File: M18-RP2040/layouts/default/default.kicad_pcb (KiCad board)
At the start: 2 copper layers, 32 x 37 mm, 39 parts

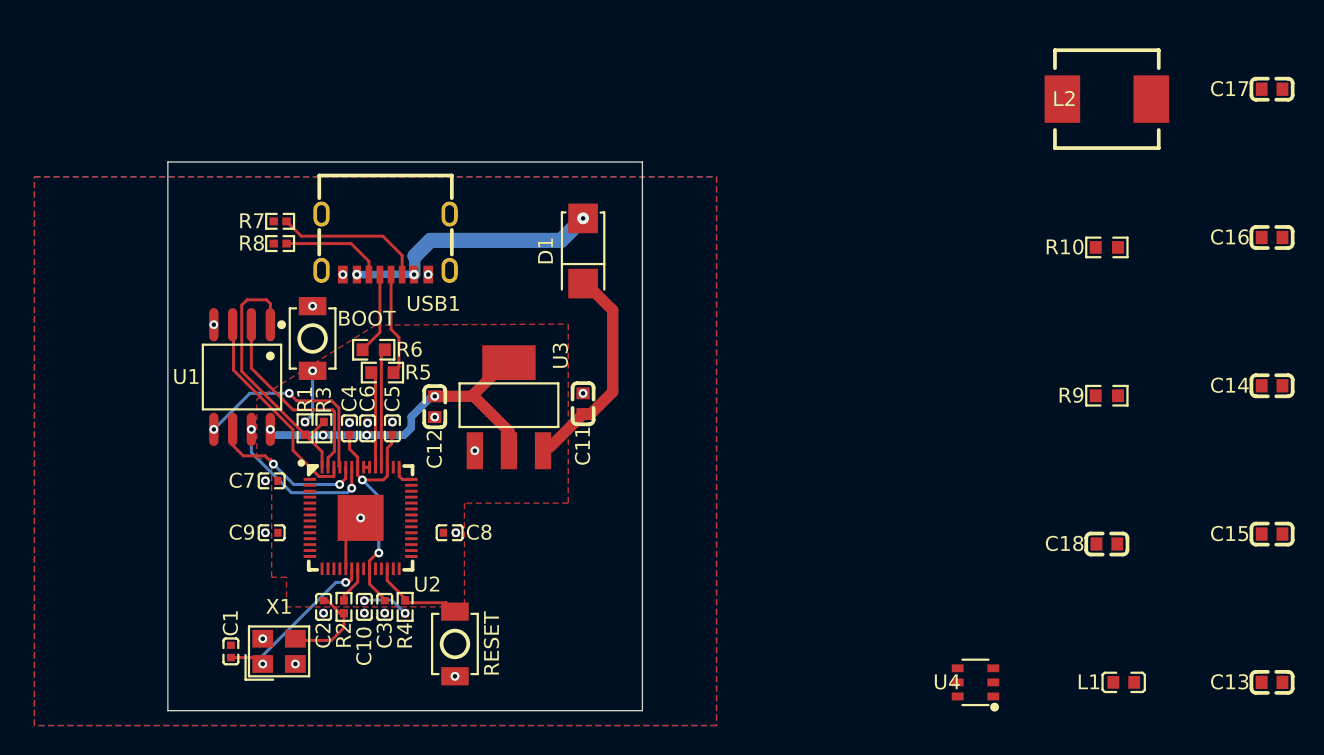
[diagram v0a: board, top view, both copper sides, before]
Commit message: M18 Buck Placement
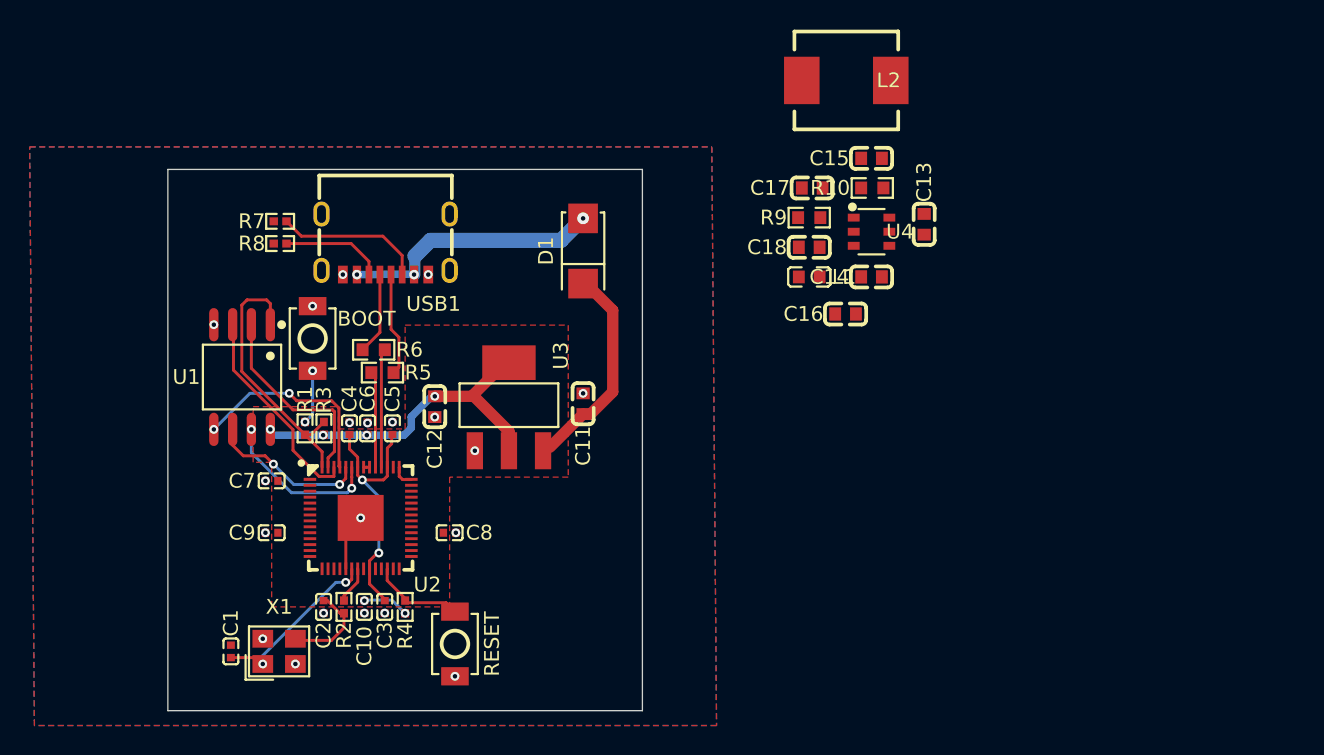
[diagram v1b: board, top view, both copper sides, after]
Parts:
- moved C13 38.8 mm to (118.0, 112.2), turned to -90 degrees
- moved C15 37.0 mm to (114.5, 107.8)
- moved L1 34.6 mm to (110.2, 115.8), turned to 180 degrees
- moved C17 31.7 mm to (110.5, 109.8)
- moved U4 31.2 mm to (114.5, 112.7), turned to 180 degrees
- moved C16 29.2 mm to (112.7, 118.2)
- moved C18 28.3 mm to (110.2, 113.8)
- moved C14 28.0 mm to (114.5, 115.8)
- moved R9 23.4 mm to (110.2, 111.8)
- moved L2 17.6 mm to (112.8, 102.5), turned to 180 degrees
- moved R10 16.3 mm to (114.5, 109.8)
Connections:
- L2 pad 1: (no net) -> lv
- L2 pad 2: (no net) -> fb_cap-power-hv
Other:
- board size 32 x 37 mm -> 32 x 36.5 mm

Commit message: Updated Buck to TI for cost savings
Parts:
- removed L1: , Murata_Electronics_BLM18PG121SN1D:L0603
- added C19: 47µF ±20%, Samsung_Electro_Mechanics_CL31A476MPHNNNE:C1206, F.Cu at (0.00, -70.0)
- added C20: 47µF ±20%, Samsung_Electro_Mechanics_CL31A476MPHNNNE:C1206, F.Cu at (0.00, -80.0)
- added C21: 10nF ±10%, Samsung_Electro_Mechanics_CL05B103KB5NNNC:C0402, F.Cu at (0.00, -110.0)
- added D2: Vf {ℝ+}V, MDD_Microdiode_Electronics_SS34:SMA_L4.3-W2.6-LS5.2-RD, F.Cu at (0.00, 0.00)
- added R11: 30kΩ ±1%, UNI_ROYAL_0603WAF3002T5E:R0603, F.Cu at (0.00, -60.0)
- added R12: 330kΩ ±1%, UNI_ROYAL_0402WGF3303TCE:R0402, F.Cu at (0.00, -90.0)
- added R13: 68kΩ ±1%, UNI_ROYAL_0402WGF6802TCE:R0402, F.Cu at (0.00, -100.0)
- C13: footprint YAGEO_CC0603KRX7R9BB104:C0603 -> Samsung_Electro_Mechanics_CL05B104KO5NNNC:C0402
- C14: value 100nF ±10% -> 10nF ±10%; footprint YAGEO_CC0603KRX7R9BB104:C0603 -> Samsung_Electro_Mechanics_CL05B103KB5NNNC:C0402
- C15: value 10µF ±10% -> 4.7µF ±10%; footprint Samsung_Electro_Mechanics_CL10A106KP8NNNC:C0603 -> FH_1206B475K500NT:C1206
- C16: value 22µF ±20% -> 4.7µF ±10%; footprint Samsung_Electro_Mechanics_CL10A226MQ8NRNC:C0603 -> FH_1206B475K500NT:C1206
- C17: value 22µF ±20% -> 47pF ±5%; footprint Samsung_Electro_Mechanics_CL10A226MQ8NRNC:C0603 -> FH_0402CG470J500NT:C0402
- C18: value 47pF ±5% -> 1nF ±10%; footprint Samsung_Electro_Mechanics_CL10C470JB8NNNC:C0603 -> FH_0402B102K500NT:C0402
- R10: value 22kΩ ±1% -> 1.8kΩ ±1%; footprint UNI_ROYAL_0603WAF2202T5E:R0603 -> UNI_ROYAL_0603WAF1801T5E:R0603
- R9: value 120kΩ ±1% -> 10kΩ ±1%; footprint UNI_ROYAL_0603WAF1203T5E:R0603 -> UNI_ROYAL_0402WGF1002TCE:R0402
- U4: footprint Diodes_Incorporated_AP63301WU_7:TSOT-23-6_L2.9-W1.6-P0.95-LS2.8-BR -> Texas_Instruments_TPS54331DR:SOIC-8_L5.0-W4.0-P1.27-LS6.0-BL
- moved C18 197.4 mm to (0.00, -50.0)
- moved C16 186.2 mm to (0.00, -30.0)
- moved C17 186.1 mm to (0.00, -40.0)
- moved C15 171.5 mm to (0.00, -20.0)
- moved C13 169.9 mm to (0.00, -10.0), turned to 0 degrees
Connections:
- C13 pad 1: bst_cap-power-hv -> boot_cap-power-hv
- C13 pad 2: lv -> cathode
- C16 pad 1: fb_cap-power-hv -> V+
- C17 pad 1: fb_cap-power-hv -> comp_c2-power-hv
- C18 pad 1: fb_cap-power-hv -> comp_c2-power-hv
- C18 pad 2: fb_cap-power-lv -> lv
- L2 pad 1: lv -> cathode
- L2 pad 2: fb_cap-power-hv -> 5V
- R10 pad 1: fb_cap-power-lv -> (no net)
- R10 pad 2: GND -> (no net)
- R9 pad 1: fb_cap-power-hv -> 5V
- R9 pad 2: fb_cap-power-lv -> VSENSE
- U4 pad 1: fb_cap-power-lv -> boot_cap-power-hv
- U4 pad 3: V+ -> EN
- U4 pad 4: GND -> ss_cap-power-hv
- U4 pad 5: lv -> VSENSE
- U4 pad 6: bst_cap-power-hv -> comp_c2-power-hv
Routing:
- net vUSB: track 17.5 -> 0.00 mm, vias 3 -> 0
- net (no net): track 0.00 -> 17.5 mm, vias 0 -> 3
- net ss_cap-power-hv: track 0.00 -> 14.5 mm
- net 5V: track 14.5 -> 0.00 mm
- net boot_cap-power-hv: track 0.00 -> 3.84 mm, vias 0 -> 20
- net GND: track 3.84 -> 0.00 mm, vias 20 -> 0
- added copper zone on B.Cu, net (none)
- added copper zone on F.Cu, net (none)
- removed copper zone on B.Cu, net GND
- removed copper zone on F.Cu, net GND

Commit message: Basic Buck layout
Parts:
- moved C21 279.0 mm to (116.0, 143.8), turned to -90 degrees
- moved R13 267.6 mm to (113.7, 142.3), turned to -90 degrees
- moved R12 256.1 mm to (113.7, 139.5), turned to -90 degrees
- moved R11 240.5 mm to (129.5, 142.6)
- moved C20 240.3 mm to (111.4, 133.0), turned to 180 degrees
- moved C18 230.2 mm to (128.8, 140.8), turned to -90 degrees
- moved C19 229.3 mm to (111.4, 130.4), turned to 180 degrees
- moved C17 222.9 mm to (130.3, 140.8), turned to -90 degrees
- moved C16 198.8 mm to (107.2, 137.4), turned to 90 degrees
- moved C15 192.8 mm to (111.3, 137.4), turned to 90 degrees
- moved D2 187.8 mm to (127.6, 137.9)
- moved C13 186.7 mm to (115.9, 136.3)
- moved R10 34.0 mm to (123.5, 142.5), turned to -90 degrees
- moved R9 33.6 mm to (125.6, 141.7), turned to 180 degrees
- moved L2 31.4 mm to (121.7, 132.6)
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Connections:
- R10 pad 1: (no net) -> VSENSE
- R10 pad 2: (no net) -> GND
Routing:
- net vUSB: track 0.00 -> 17.5 mm, vias 0 -> 3
- net (no net): track 17.5 -> 0.00 mm, vias 3 -> 0
- net ss_cap-power-hv: track 14.5 -> 0.00 mm
- net 5V: track 0.00 -> 14.5 mm
- net boot_cap-power-hv: track 3.84 -> 0.00 mm, vias 20 -> 0
- net GND: track 0.00 -> 3.84 mm, vias 0 -> 20

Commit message: Build clean up and buck routing
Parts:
- moved C13 12.7 mm to (103.2, 135.5)
- moved C21 12.7 mm to (103.3, 142.9)
- moved D2 12.7 mm to (114.8, 137.0)
- moved L2 12.7 mm to (109.0, 131.8)
- moved R10 12.7 mm to (110.8, 141.7)
- moved R12 12.7 mm to (101.0, 138.7)
- moved R13 12.7 mm to (101.0, 141.4)
- moved R9 12.7 mm to (112.9, 140.8)
- moved U4 12.7 mm to (106.0, 138.8)
- moved C17 12.7 mm to (117.6, 140.0)
- moved C18 12.7 mm to (116.1, 140.0)
- moved R11 12.7 mm to (116.8, 141.8)
- moved C14 12.7 mm to (96.6, 137.0)
- moved C15 12.7 mm to (98.6, 137.0)
- moved C16 12.7 mm to (94.5, 137.0)
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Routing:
- net V+: track 0.00 -> 50.5 mm
- net 5V: track 14.5 -> 49.6 mm
- net cathode: track 0.00 -> 17.9 mm
- net comp_c2-power-hv: track 0.00 -> 8.91 mm
- net GND: track 3.84 -> 10.3 mm, vias 20 -> 28
- net EN: track 0.00 -> 4.39 mm
- net vUSB: track 17.5 -> 13.2 mm
- net VSENSE: track 0.00 -> 3.85 mm
- net c_osc_2-power-hv: track 6.38 -> 4.06 mm
- net hv: track 11.7 -> 9.80 mm
- net ss_cap-power-hv: track 0.00 -> 1.77 mm
- net boot_cap-power-hv: track 0.00 -> 1.69 mm
- net lv: track 0.00 -> 1.41 mm
- added copper zone on B.Cu, net GND
- added copper zone on F.Cu, net GND
- removed copper zone on B.Cu, net (none)
- removed copper zone on F.Cu, net (none)
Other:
- board size 32 x 36.5 mm -> 70 x 36 mm

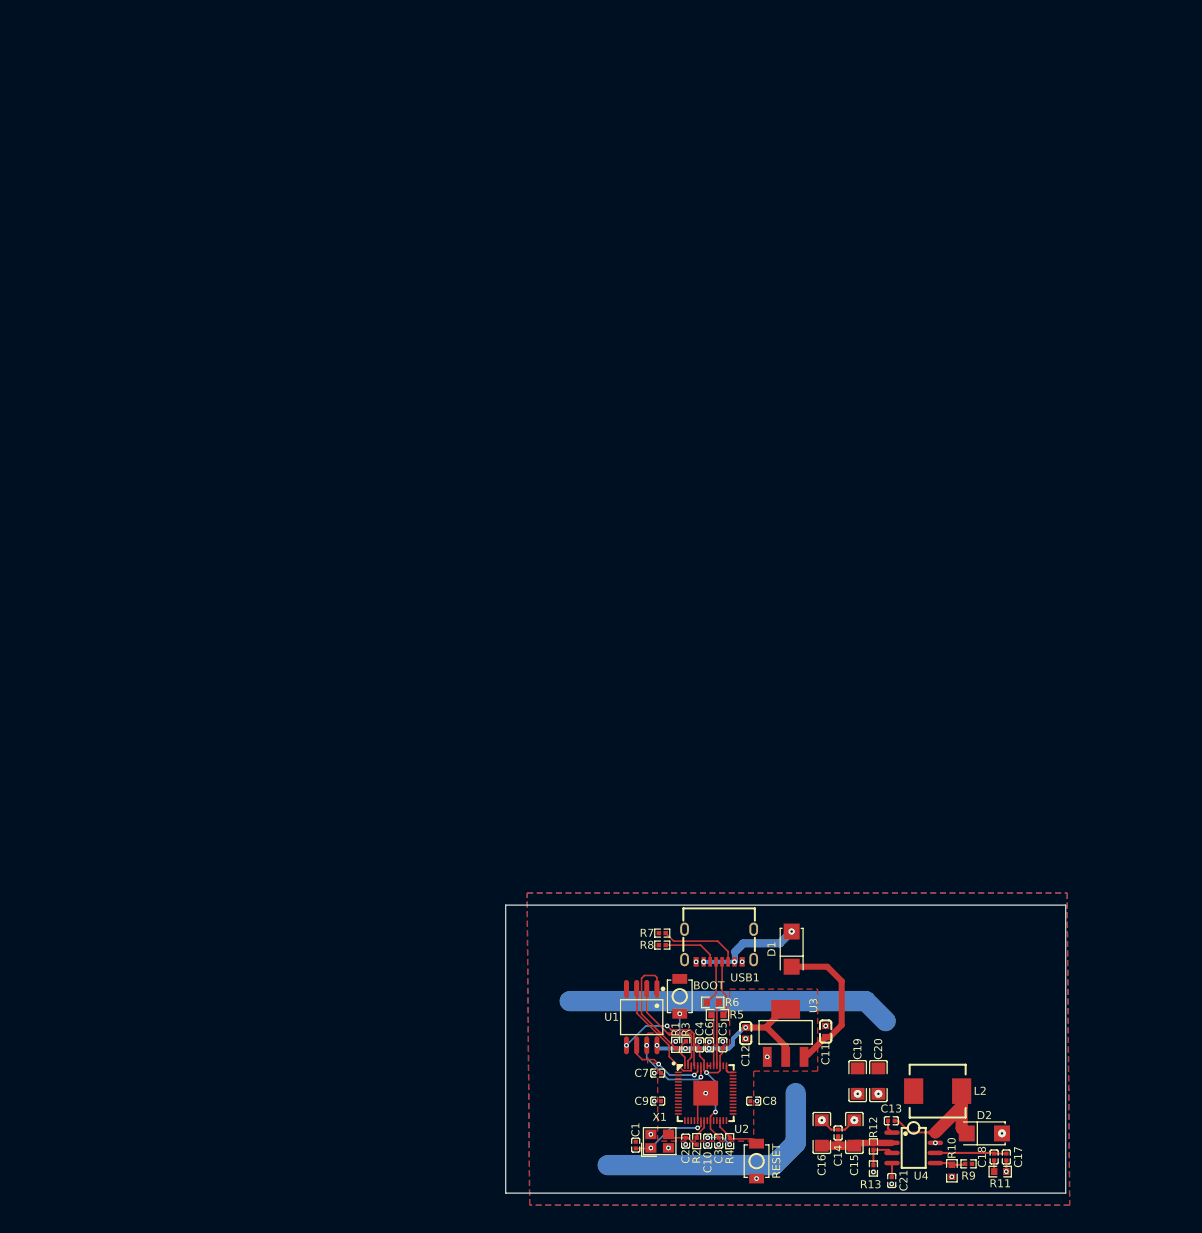
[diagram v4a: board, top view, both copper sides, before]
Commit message: ESP32 New Buck & Header Updates
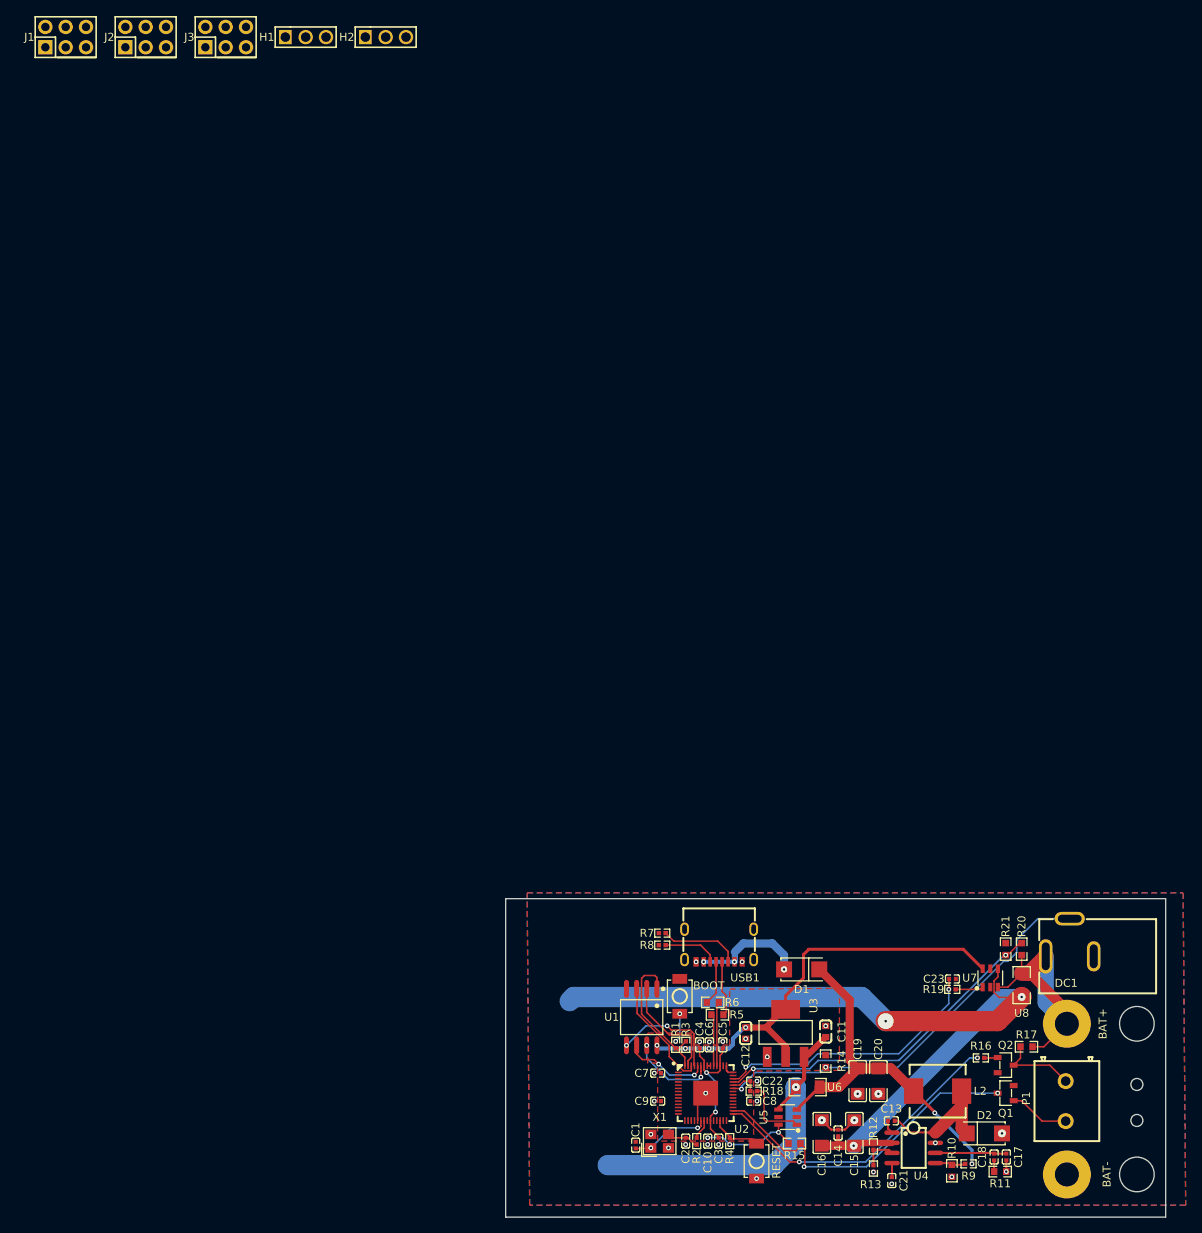
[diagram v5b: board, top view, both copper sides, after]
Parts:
- added BAT+: , m18_10awg_pad:M18_10AWG_PAD, F.Cu at (125.2, 123.3)
- added BAT-: , m18_10awg_pad:M18_10AWG_PAD, F.Cu at (125.2, 142.2)
- added C22: 10nF ±10%, Samsung_Electro_Mechanics_CL05B103KB5NNNC:C0402, F.Cu at (86.0, 130.5)
- added C23: 10nF ±10%, Samsung_Electro_Mechanics_CL05B103KB5NNNC:C0402, F.Cu at (110.8, 117.7)
- added DC1: , CUI_PJ_002BH:DC-IN-TH_PJ-002BH, F.Cu at (125.5, 112.5)
- added H1: , BOOMELE_2_54_1_3P:HDR-TH_3P-P2.54-V-M-1, F.Cu at (30.0, 0.00)
- added H2: , BOOMELE_2_54_1_3P:HDR-TH_3P-P2.54-V-M-1, F.Cu at (40.0, 0.00)
- added J1: , BOOMELE_2_54_2_3P:HDR-TH_6P-P2.54-V-M-R2-C3-S2.54-1, F.Cu at (0.00, 0.00)
- added J2: , BOOMELE_2_54_2_3P:HDR-TH_6P-P2.54-V-M-R2-C3-S2.54-1, F.Cu at (10.0, 0.00)
- added J3: , BOOMELE_2_54_2_3P:HDR-TH_6P-P2.54-V-M-R2-C3-S2.54-1, F.Cu at (20.0, 0.00)
- added P1: , Ningbo_Kangnex_Elec_WJ127_5_0_02P_14_00A:CONN-TH_2P-P5.00_CPC3703CTR, F.Cu at (125.0, 133.0)
- added Q1: , Changjiang_Electronics_Tech_2N7002:SOT-23-3_L2.9-W1.3-P1.90-LS2.4-BR, F.Cu at (117.5, 132.0)
- added Q2: , Changjiang_Electronics_Tech_2N7002:SOT-23-3_L2.9-W1.3-P1.90-LS2.4-BR, F.Cu at (117.5, 128.5)
- added R14: 10kΩ ±1%, UNI_ROYAL_0603WAF1002T5E:R0603, F.Cu at (95.0, 128.0)
- added R15: 10kΩ ±1%, UNI_ROYAL_0603WAF1002T5E:R0603, F.Cu at (91.1, 138.3)
- added R16: 330Ω ±1%, UNI_ROYAL_0402WGF3300TCE:R0402, F.Cu at (114.4, 127.6)
- added R17: 10kΩ ±1%, UNI_ROYAL_0603WAF1002T5E:R0603, F.Cu at (120.1, 126.2)
- added R18: 220Ω ±1%, UNI_ROYAL_0402WGF2200TCE:R0402, F.Cu at (86.0, 131.8)
- added R19: 220Ω ±1%, UNI_ROYAL_0402WGF2200TCE:R0402, F.Cu at (110.8, 119.0)
- added R20: 150kΩ ±1%, UNI_ROYAL_0603WAF1503T5E:R0603, F.Cu at (119.5, 114.0)
- added R21: 22kΩ ±1%, UNI_ROYAL_0603WAF2202T5E:R0603, F.Cu at (117.5, 114.0)
- added U5: , Texas_Instruments_INA181A2IDBVR:SOT-23-6_L2.9-W1.6-P0.95-LS2.8-BL, F.Cu at (90.2, 135.0)
- added U6: , FOJAN_FRM121WFR010TM:R1206, F.Cu at (92.8, 131.2)
- added U7: , Texas_Instruments_INA181A2IDBVR:SOT-23-6_L2.9-W1.6-P0.95-LS2.8-BL, F.Cu at (115.6, 117.6)
- added U8: , FOJAN_FRM121WFR010TM:R1206, F.Cu at (119.5, 118.5)
- C1, C2: value 22pF ±5% -> 20pF ±20%
- C10, C3, C4, C5, C6, C7, C8, C9: value 1µF ±10% -> 1µF ±20%
- C11: value 10µF ±10% -> 10µF ±20%
- C15, C16: value 4.7µF ±10% -> 4.7µF ±20%
- R1, R2: value 1kΩ ±1% -> 1kΩ ±5%
- R10: value 1.8kΩ ±1% -> {ℝ+}Ω
- R3, R4: value 10kΩ ±1% -> 10kΩ ±5%
- R5, R6: value 22Ω ±1% -> 22Ω ±5%
- R7, R8: value 5.1kΩ ±1% -> 5.1kΩ ±5%
- R9: value 10kΩ ±1% -> {ℝ+}Ω
- moved D1 2.83 mm to (92.0, 116.5), turned to 180 degrees
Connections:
- C1 pad 1: hv -> c_osc_1-power-hv
- C19 pad 1: 5V -> 5Vin
- C20 pad 1: 5V -> 5Vin
- D1 pad 1: 5V -> 5Vin
- L2 pad 2: 5V -> 5Vin
- R9 pad 1: 5V -> 5Vin
- U2 pad 2: gpio0 -> 3
- U2 pad 20: hv -> c_osc_1-power-hv
- U2 pad 3: gpio1 -> 4
- U2 pad 30: gpio19 -> D
- U2 pad 37: gpio25 -> 3-2
- U2 pad 38: gpio26_a0 -> hv
- U2 pad 4: gpio2 -> 3-1
- U2 pad 40: gpio28_a2 -> vin_sense_c1-power-hv
- U2 pad 5: gpio3 -> 4-1
- U2 pad 8: gpio6 -> 2
- X1 pad 1: hv -> c_osc_1-power-hv
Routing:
- net 57: track 0.00 -> 104.8 mm, vias 0 -> 3
- net 3-2: track 0.00 -> 52.1 mm, vias 0 -> 2
- net V+: track 50.5 -> 0.00 mm
- net 5V: track 49.6 -> 0.00 mm
- net 5Vin: track 0.00 -> 44.4 mm, vias 0 -> 2
- net gpio27_a1: track 0.00 -> 43.3 mm, vias 0 -> 2
- net 60: track 0.00 -> 43.2 mm, vias 0 -> 1
- net D: track 0.00 -> 42.8 mm, vias 0 -> 2
- net 3V3: track 28.8 -> 69.9 mm, vias 6 -> 7
- net gpio18: track 0.00 -> 38.4 mm, vias 0 -> 2
- net vin_sense_c1-power-hv: track 0.00 -> 34.4 mm, vias 0 -> 2
- net VIN: track 0.00 -> 34.3 mm
- net DP: track 0.00 -> 9.98 mm
- net c_osc_1-power-hv: track 0.00 -> 9.80 mm, vias 0 -> 2
- net OUT: track 0.00 -> 8.61 mm
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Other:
- board size 70 x 36 mm -> 82.5 x 39.8 mm
